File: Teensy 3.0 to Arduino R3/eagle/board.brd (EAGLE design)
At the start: 100 x 55.9 mm, 43 parts, among them IC1 7805TV, IC2 24AA256SN, IC3 24AA256SN, IC4 24AA256SN, IC5 24AA256SN, U1 MICROSD

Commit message: Version 3 final
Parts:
- added C9: (no value), resistor:PANASONIC_D
- added D2: (no value), SparkFun-DiscreteSemi:SMA-DIODE-KIT
- added R10, R11, R12, R13, R14, R15, R16, R17, R18, R19, R20, R21, R22, R23, R24, R5, R6, R7, R8, R9: (no value), resistor:R0805
- added SJ3, SJ4, SJ5, SJ6: (no value), SparkFun-Passives:SJ_2S-NO
- IC1: value 7805TV -> 78XX compatible
- SJ1, SJ2: value SOLDERJUMPERNO -> (none)
- moved SJ2 10.0 mm to (25.4, 39.4)
- moved SJ1 8.47 mm to (20.3, 38.1), turned to 180 degrees
- moved F1 4.62 mm to (17.1, 33.0), turned to 270 degrees
- moved C2 2.62 mm to (27.9, 31.8)
- moved D1 1.27 mm to (21.6, 43.2)
- moved IC1 1.27 mm to (34.3, 38.1)
- moved C1 1.27 mm to (25.4, 43.8)
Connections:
- removed net 3V3: C2.+, C4.1, C5.1, C6.1, C7.1, C8.1, IC1.3, IC2.3, IC2.8, IC3.2, IC3.3, IC3.8, IC4.1, IC4.3, IC4.8, IC5.1, IC5.2, IC5.3, IC5.8, JP12.1, JP13.13, JP14.1, JP6.5, JP6.7, R1.2, R2.2, R3.2, R4.2, SJ2.1, U1.4
- new net N$10: JP2.7, R10.2
- new net N$11: JP2.6, R11.2
- new net N$12: JP2.5, R12.2
- new net N$13: JP1.13, R13.2
- new net N$14: JP1.12, R14.2
- new net N$15: JP1.11, R15.2
- new net N$16: JP1.10, R16.2
- new net N$17: JP1.9, R17.2
- new net N$18: JP1.8, R18.2
- new net N$19: JP1.7, R19.2
- new net N$20: JP1.6, R20.2
- new net N$21: JP2.4, R21.2
- new net N$22: JP2.3, R22.2
- new net N$23: JP2.2, R23.2
- new net N$24: JP2.1, R24.2
- new net N$5: JP1.5, R5.2
- new net N$6: JP1.4, R6.2
- new net N$7: JP1.3, R7.2
- new net N$8: JP1.2, R8.2
- new net N$9: JP1.1, R9.2
- new net NIC: R4.1, SJ3.1, SJ4.1, U1.CD1
- new net QW: SJ5.1, SJ6.1, U1.2
- net 3.3V: now also C2.+, C4.1, C5.1, C6.1, C7.1, C8.1, C9.+, D2.A, IC1.3, IC2.3, IC2.8, IC3.2, IC3.3, IC3.8, IC4.1, IC4.3, IC4.8, IC5.1, IC5.2, IC5.3, IC5.8, JP12.1, JP13.13, JP14.1, JP6.5, JP6.7, R1.2, R2.2, R3.2, R4.2, SJ2.1, U1.4
- net A0: now also R23.1; no longer JP2.2
- net A1: now also R22.1; no longer JP2.3
- net A2: now also R21.1; no longer JP2.4
- net A3: now also R12.1; no longer JP2.5
- net A4: now also R11.1; no longer JP2.6
- net A5: now also R10.1; no longer JP2.7
- net D0: now also R13.1; no longer JP1.13
- net D1: now also R14.1; no longer JP1.12
- net D10: now also R7.1, SJ6.2; no longer JP1.3, U1.2
- net D11: now also R8.1; no longer JP1.2
- net D12: now also R9.1; no longer JP1.1
- net D13: now also R24.1; no longer JP2.1
- net D2: now also R15.1; no longer JP1.11
- net D3: now also R16.1; no longer JP1.10
- net D4: now also R17.1; no longer JP1.9
- net D5: now also R18.1; no longer JP1.8
- net D6: now also R19.1; no longer JP1.7
- net D7: now also R20.1, SJ3.2; no longer JP1.6
- net D8: now also R5.1, SJ4.2; no longer JP1.5, R4.1, U1.CD1
- net D9: now also R6.1, SJ5.2; no longer JP1.4
- net GND: now also C9.-
- net N$3: now also D2.C
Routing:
- net 3.3V: track 0.00 -> 400.0 mm, vias 0 -> 7
- net 3V3: track 390.8 -> 0.00 mm, vias 7 -> 0
- net QW: track 0.00 -> 51.5 mm, vias 0 -> 2
- net NIC: track 0.00 -> 51.1 mm, vias 0 -> 5
- net D8: track 73.9 -> 23.0 mm, vias 5 -> 0
- net D10: track 62.2 -> 23.2 mm, vias 2 -> 0
- net A1: track 29.0 -> 6.03 mm
- net N$22: track 0.00 -> 21.6 mm
- net A3: track 29.0 -> 16.2 mm
- net N$11: track 0.00 -> 12.4 mm
- net A2: track 29.0 -> 16.8 mm
- net N$12: track 0.00 -> 11.1 mm
- net N$21: track 0.00 -> 10.5 mm
- net N$10: track 0.00 -> 9.84 mm
- net D13: track 119.5 -> 113.1 mm
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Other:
- board text added: "-"
- board text added: "D10"
- board text added: "D7"
- board text added: "D8"
- board text added: "D9"
- board text added: "PROGRAM"
- board text added: "SD Card CS"
- board text added: "SD Card dedect"

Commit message: V3-2: fixed several bugs
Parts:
- added C10: (no value), rcl:SANYO-OSCON_SMD_E7
- added JP16: (no value), SparkFun-Connectors:1X02
- C3: device SparkFun-Capacitors:EIA3528-KIT -> rcl:A/3216-18W
- moved C3 17.1 mm to (20.3, 5.08), turned to 90 degrees
- moved R22 16.7 mm to (45.7, 7.62), turned to 90 degrees
- moved F2 7.24 mm to (8.89, 12.1), turned to 180 degrees
- moved JP15 3.42 mm to (3.81, 13.3), turned to 270 degrees
- moved R23 3.18 mm to (39.4, 8.89)
- moved JP6 2.54 mm to (61.0, 3.81)
- moved JP10 1.91 mm to (5.08, 24.8)
- moved X1 1.27 mm to (6.99, 36.8)
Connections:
- new net N$25: C10.+, JP16.2
- net GND: now also C10.-, C3.-; no longer C3.C
- net N$2: now also JP16.1
- net VUSB: now also C3.+; no longer C3.A
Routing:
- net VUSB: track 149.5 -> 128.5 mm, vias 2 -> 0
- net N$22: track 21.6 -> 2.96 mm
- net A1: track 6.03 -> 24.3 mm
- net N$25: track 0.00 -> 8.46 mm
- net GND: track 20.5 -> 14.9 mm, vias 40 -> 42
- net VIN: track 129.7 -> 135.3 mm
- net A0: track 47.8 -> 44.7 mm
- net EXT_RESET: track 51.5 -> 54.1 mm
- net 5V: track 15.0 -> 17.6 mm
- net N$2: track 4.02 -> 6.50 mm
- net N$23: track 2.63 -> 4.91 mm
- net N$1: track 28.4 -> 26.5 mm
- net N$3: track 49.5 -> 47.9 mm
- net PROG: track 104.6 -> 103.2 mm
- net EXT_POWER: track 32.2 -> 33.5 mm
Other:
- board text added: "A4 SDA"
- board text added: "A5 SCL"
- board text added: "MISO 12"
- board text added: "MOSI 11"
- board text added: "PWM 3"
- board text added: "PWM 4"
- board text added: "PWM 5"
- board text added: "PWM 6"
- board text added: "PWM RX2 CS1 9"
- board text added: "PWM TX2 CS0 10"
- board text added: "RX1 0"
- board text added: "RX3 7"
- board text added: "SCK 13"
- board text added: "TX1 1"
- board text added: "TX3 8"
- board text added: "V000003-2 tinytiger.ch"
- board text removed: "0"
- board text removed: "1"
- board text removed: "10"
- board text removed: "11"
- board text removed: "12"
- board text removed: "13"
- board text removed: "3"
- board text removed: "4"
- board text removed: "5"
- board text removed: "6"
- board text removed: "7"
- board text removed: "8"
- board text removed: "9"
- board text removed: "A4"
- board text removed: "A5"
- board text removed: "C3"
- board text removed: "F2"
- board text removed: "V000003 tinytiger.ch"

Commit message: inital commit V4
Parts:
- removed JP14: (no value), SparkFun-Connectors:1X02
- added JP17, JP18: M10", SparkFun-Connectors:1X10
- added R25, R26, R27, R28, R29, R30, R31, R32, R33, R34, R35, R36, R37, R38, R39, R40, R41, R42: (no value), resistor:R0805
- added SJ10, SJ11, SJ12, SJ13, SJ7, SJ8, SJ9: (no value), SparkFun-Passives:SJ_2S-NO
- added U$1: XBEE-1B2, SparkFun-RF:XBEE-SILK
- added U$3, U$4: M24, SparkFun-Connectors:1X24
- C10: device rcl:SANYO-OSCON_SMD_E7 -> rcl:085CS_1AR
- C3: device rcl:A/3216-18W -> rcl:CT3528
- JP12: value (none) -> PINHD-1X10; device adafruit:1X13-BIG -> adafruit:1X10-BIG
- JP13: device adafruit:1X13-BIG -> adafruit:1X08-BIG
- JP16: device SparkFun-Connectors:1X02 -> SparkFun-Connectors:1X05
- JP2: value M14 -> (none); device SparkFun-Connectors:1X14 -> pinhead:2X06
- JP3: value M10" -> M14; device SparkFun-Connectors:1X10 -> SparkFun-Connectors:1X14
- JP4: value M10" -> (none); device SparkFun-Connectors:1X10 -> pinhead:2X06
- moved CN2 106.1 mm to (102.2, 66.0), turned to 90 degrees
- moved S1 96.8 mm to (95.2, 36.8), turned to 270 degrees
- moved JP10 95.5 mm to (86.4, 74.9), turned to 0 degrees
- moved X1 87.7 mm to (92.7, 55.2), turned to 90 degrees
- moved CN1 82.1 mm to (89.5, 55.2), turned to 270 degrees
- moved JP8 80.2 mm to (47.0, 77.5), turned to 0 degrees
- moved F1 79.9 mm to (95.9, 46.4)
- moved JP6 73.8 mm to (64.8, 77.5), turned to 0 degrees
- moved R13 73.3 mm to (5.71, 64.1), turned to 180 degrees
- moved R3 73.0 mm to (90.2, 38.1), flipped to the bottom
- moved D1 69.9 mm to (91.4, 46.4)
- moved R14 69.9 mm to (5.71, 61.6), turned to 180 degrees
- moved SJ1 68.5 mm to (88.3, 47.0), turned to 90 degrees
- moved JP15 66.8 mm to (32.4, 73.7), turned to 90 degrees
- moved R15 66.5 mm to (5.71, 59.1), turned to 180 degrees
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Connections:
- new net N$26: JP17.9, R26.2
- new net N$27: JP17.8, R27.2
- new net N$28: JP17.7, R28.2
- new net N$29: JP17.6, R29.2
- new net N$30: JP17.5, R30.2
- new net N$31: JP17.4, R31.2
- new net N$32: JP17.3, R32.2
- new net N$33: JP17.2, R33.2
- new net N$34: JP17.1, R34.2
- new net N$35: JP3.11, R35.2
- new net N$36: JP3.10, R36.2
- new net N$37: JP3.9, R37.2
- new net N$38: JP3.8, R38.2
- new net N$39: JP18.4, R39.2
- new net N$40: JP18.3, R40.2
- new net N$41: JP18.2, R41.2
- new net N$42: JP18.1, R42.2
- new net N$45: JP13.6, U$1.4
- new net N$46: JP13.5, U$1.5
- new net N$47: JP13.4, U$1.6
- new net N$48: JP13.3, U$1.7
- new net N$49: JP13.2, U$1.8
- new net N$50: JP13.1, U$1.9
- new net N$51: JP12.1, U$1.20
- new net N$52: JP4.10, JP4.9, SJ10.1, SJ11.1, SJ12.1, SJ9.1
- new net N$53: JP4.11, JP4.12
- new net N$54: JP12.2, U$1.19
- new net N$55: JP12.3, U$1.18
- new net N$56: JP12.4, U$1.17
- new net N$57: JP2.7, JP2.8
- new net N$58: JP2.10, JP2.9
- new net N$59: JP12.5, U$1.16
- new net N$60: JP12.6, U$1.15
- new net N$61: JP12.7, U$1.14
- new net N$62: JP12.8, U$1.13
- new net N$63: JP12.9, U$1.12
- new net N$64: JP12.10, U$1.11
- net 3.3V: now also JP16.4, JP2.3, JP2.4, JP2.5, JP2.6, JP3.12, SJ13.1, U$1.1, U$4.23; no longer JP12.1, JP13.13, JP14.1, JP2.12
- net 5V: now also SJ13.2; no longer JP14.2
- net A0: now also U$4.13
- net A1: now also U$4.14
- net A10: now also R42.1, U$4.2; no longer JP13.6, JP4.1
- net A11: now also R41.1, U$4.3; no longer JP13.7, JP4.2
- net A12: now also R40.1, U$4.4; no longer JP13.8, JP4.3
- net A13: now also R39.1, U$4.5; no longer JP13.9, JP4.4
- net A2: now also U$4.15
- net A3: now also U$4.16
- net A4: now also U$4.17
- net A5: now also U$4.18
- net A6: now also R38.1, U$4.19; no longer JP13.2, JP2.8
- net A7: now also R37.1, U$4.20; no longer JP13.3, JP2.9
- net A8: now also R36.1, U$4.21; no longer JP13.4, JP2.10
- net A9: now also R35.1, U$4.22; no longer JP13.5, JP2.11
- net AGND: now also JP3.13, U$4.24; no longer JP12.12, JP2.13
- net AREF: now also JP18.6, U$4.7; no longer JP4.6
- net D0: now also JP13.8, U$1.2, U$3.24
- net D1: now also JP13.7, U$1.3, U$3.23
- net D10: now also SJ10.2, U$3.14
- net D11: now also JP2.11, JP2.12, JP4.5, JP4.6, U$3.13
- net D12: now also U$3.12
- net D13: now also JP4.7, JP4.8, U$4.12
- net D2: now also SJ11.2, SJ7.2, U$3.22
- net D24: now also R25.1, U$3.11; no longer JP12.2, JP3.10
- net D25: now also R26.1, U$3.10; no longer JP12.3, JP3.9
- net D26: now also R27.1, U$3.9; no longer JP12.4, JP3.8
- net D27: now also R28.1, U$3.8; no longer JP12.5, JP3.7
- net D28: now also R29.1, U$3.7; no longer JP12.6, JP3.6
- net D29: now also R30.1, U$3.6; no longer JP12.7, JP3.5
- net D3: now also SJ12.2, SJ8.2, U$3.21
- net D30: now also R31.1, U$3.5; no longer JP12.8, JP3.4
- net D31: now also R32.1, U$3.4; no longer JP12.9, JP3.3
- net D32: now also R33.1, U$3.3; no longer JP12.10, JP3.2
- net D33: now also R34.1, U$3.2; no longer JP12.11, JP3.1
- net D4: now also U$3.20
- net D5: now also U$3.19
- net D6: now also U$3.18
- net D7: now also U$3.17
- net D8: now also U$3.16
- net D9: now also SJ9.2, U$3.15
- net GND: now also JP16.3, JP18.9, JP2.1, JP2.2, JP4.1, JP4.2, JP4.3, JP4.4, U$1.10, U$3.25, U$4.10; no longer JP12.13, JP13.1, JP4.9
- net N$10: now also JP3.7; no longer JP2.7
- net N$11: now also JP3.6; no longer JP2.6
- net N$12: now also JP3.5; no longer JP2.5
- net N$2: now also C10.+; no longer JP16.1
- net N$21: now also JP3.4; no longer JP2.4
- net N$22: now also JP3.3; no longer JP2.3
- net N$23: now also JP3.2; no longer JP2.2
- net N$24: now also JP3.1; no longer JP2.1
- net N$25: now also JP17.10, R25.2; no longer C10.+, JP16.2
- net PROG: now also JP16.2, JP18.5, U$4.6; no longer JP13.10, JP4.5
- net QW: now also SJ7.1, SJ8.1
- net RESET: now also JP16.1, JP18.7, U$4.8; no longer JP4.7
- net VBAT: now also JP16.5, JP18.10, U$4.11; no longer JP13.12, JP4.10
- net VIN: now also JP3.14, U$4.25; no longer JP2.14
- net VUSB: now also JP18.8, U$4.9; no longer JP13.11, JP4.8
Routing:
- net D0: track 23.3 -> 196.9 mm, vias 0 -> 5
- net D3: track 23.3 -> 167.9 mm, vias 0 -> 7
- net D9: track 22.6 -> 146.2 mm, vias 0 -> 5
- net D8: track 23.0 -> 133.6 mm, vias 0 -> 4
- net D1: track 23.3 -> 133.6 mm, vias 0 -> 5
- net N$45: track 0.00 -> 109.8 mm, vias 0 -> 4
- net D11: track 101.1 -> 202.4 mm
- net D33: track 90.3 -> 2.96 mm
- net D10: track 23.2 -> 109.7 mm, vias 0 -> 7
- net D32: track 85.9 -> 2.96 mm
- net A13: track 85.2 -> 2.96 mm, vias 2 -> 0
- net A11: track 84.4 -> 2.96 mm, vias 2 -> 0
- net A10: track 84.4 -> 2.96 mm, vias 1 -> 0
- net A12: track 83.7 -> 2.96 mm, vias 2 -> 0
- net D4: track 23.3 -> 102.2 mm, vias 0 -> 3
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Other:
- board size 100 x 55.9 mm -> 100 x 80 mm
- board text added: "GND 0 1 2 3 4 5 6 7 8 9 10 11 12 24 25 26 27 28 29 30 31 32 33"
- board text added: "REV. V000004"
- board text added: "Teensy 3.0"
- board text added: "VIN AGND 3V3 A9 A8 A7 A6 A5 A4 A3 A2 A1 A0 13 VBAT GND VUSB RST AREF PRG A13 A12 A11 A10"
- board text added: "WIZ820io"
- board text added: "XBee"
- board text added: "github.com/thewknd/Teensy3.0ToArduinoR3"
- board text added: "tinytiger.ch"
- board text removed: "24"
- board text removed: "25"
- board text removed: "26"
- board text removed: "27"
- board text removed: "28"
- board text removed: "29"
- board text removed: "30"
- board text removed: "31"
- board text removed: "32"
- board text removed: "33"
- board text removed: "A10"
- board text removed: "A11"
- board text removed: "A12"
- board text removed: "A13"
- board text removed: "A6"
- board text removed: "A7"
- board text removed: "A8"
- board text removed: "A9"
- board text removed: "AGND"
- board text removed: "C1"
- board text removed: "D1"
- board text removed: "D10"
- board text removed: "D7"
- board text removed: "D8"
- board text removed: "D9"
- board text removed: "I2C Pullup"
- board text removed: "PROG"
- board text removed: "PROGRAM"
- board text removed: "REG."
- board text removed: "RESET"
- board text removed: "SD Card CS"
- board text removed: "SD Card dedect"
- board text removed: "SJ1"
- board text removed: "SJ2"
- board text removed: "V000003-2 tinytiger.ch"
- board text removed: "VBAT"
- board text removed: "VUSB"

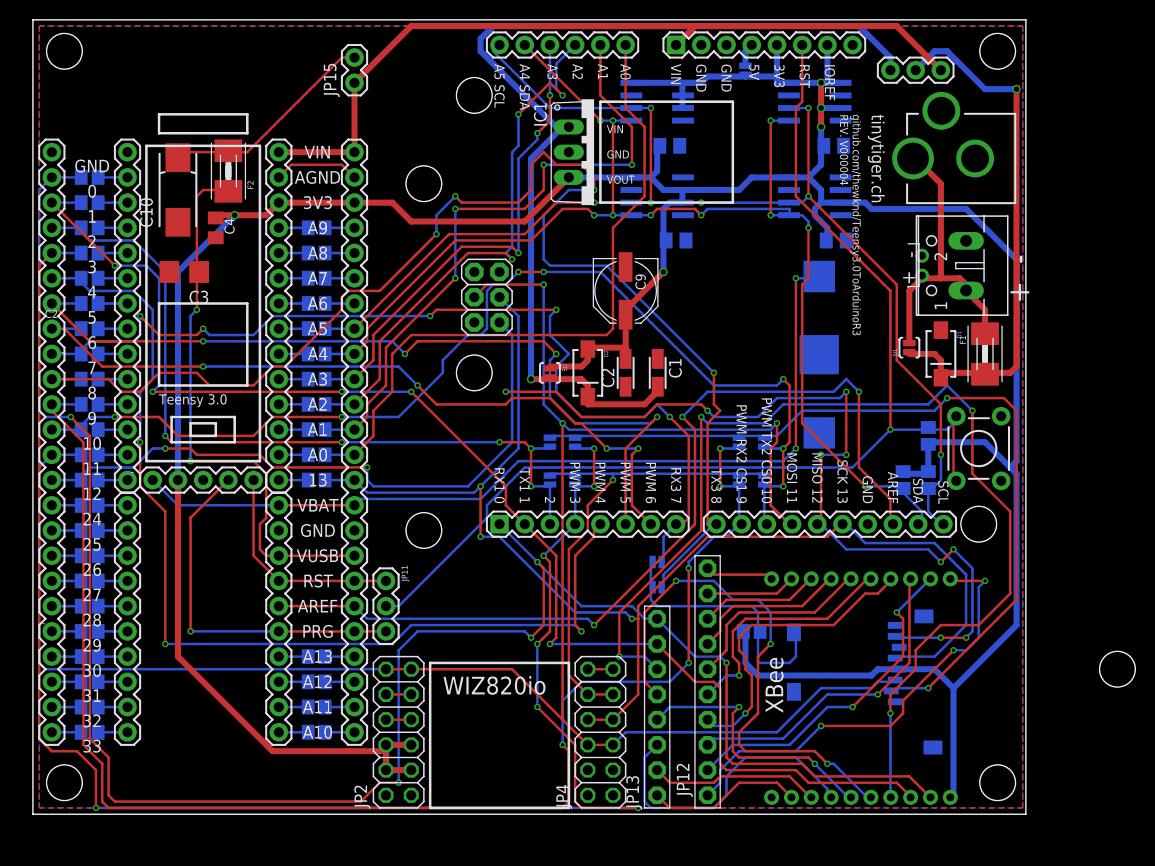
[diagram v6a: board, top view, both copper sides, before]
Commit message: -added RS485 transceiver
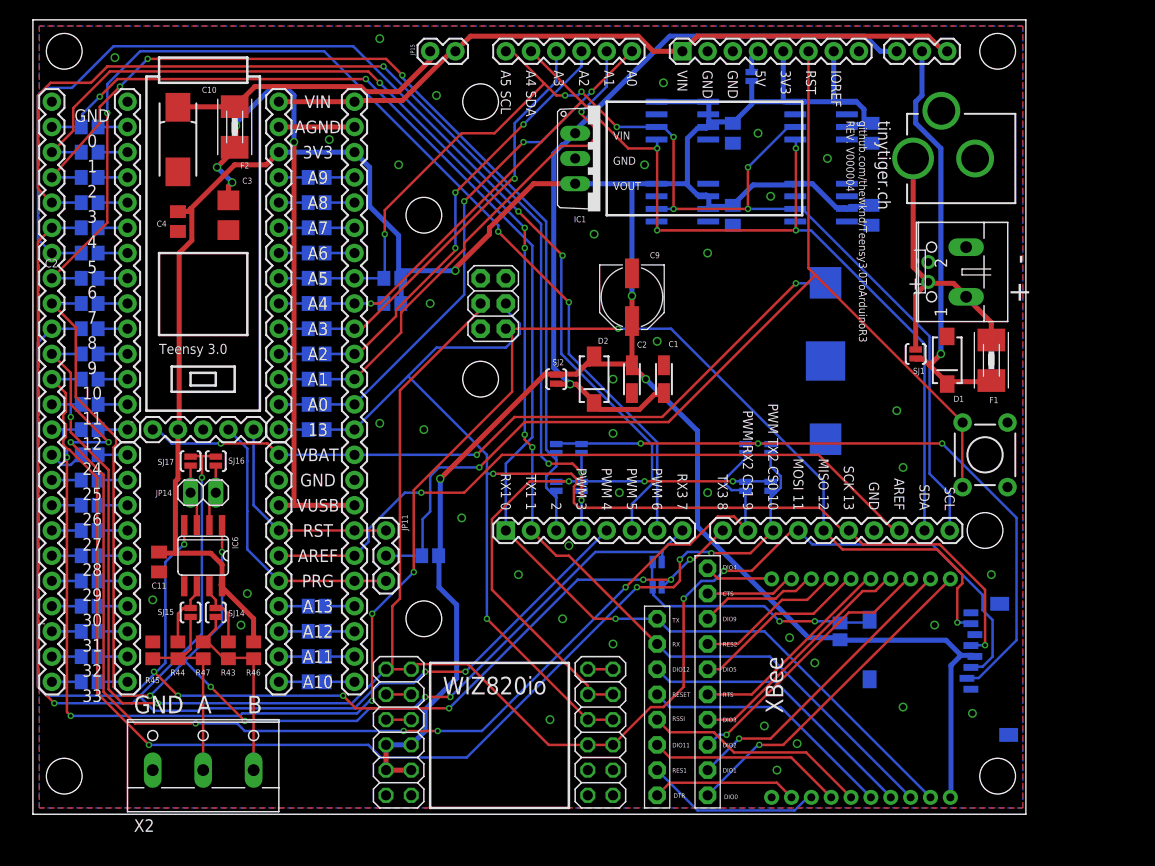
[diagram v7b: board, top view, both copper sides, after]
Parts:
- added C11: (no value), rcl:C0805K
- added IC6: LTC2862, maxim:SO08
- added JP14: (no value), pinhead:1X02
- added R43, R44, R45, R46, R47: (no value), resistor:R0805
- added SJ14, SJ15, SJ16, SJ17: (no value), SparkFun-Passives:SJ_2S-NO
- added X2: (no value), con-wago-508:W237-133
- moved R2 57.7 mm to (36.2, 54.0), turned to 180 degrees
- moved R1 54.4 mm to (36.2, 51.4), turned to 180 degrees
- moved R3 51.6 mm to (40.0, 26.0), turned to 180 degrees
- moved JP15 10.6 mm to (42.5, 76.8), turned to 180 degrees
- moved R4 8.89 mm to (81.3, 18.4), turned to 270 degrees
- moved U1 7.73 mm to (83.8, 21.6)
- moved C3 7.24 mm to (19.7, 60.3), turned to 270 degrees
- moved C8 6.48 mm to (70.5, 68.6), turned to 270 degrees
- moved C6 6.25 mm to (70.5, 60.3), turned to 270 degrees
- moved R11 5.08 mm to (28.6, 51.4)
- moved R12 5.08 mm to (28.6, 48.9)
- moved R15 5.08 mm to (5.71, 64.1)
- moved R20 5.08 mm to (5.71, 51.4)
- moved R35 5.08 mm to (28.6, 64.1)
- moved R5 5.08 mm to (5.71, 48.9)
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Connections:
- new net N$43: IC6.2, JP14.2, SJ16.2
- new net N$44: IC6.3, JP14.1, SJ17.2
- new net N$65: IC6.7, R43.1, SJ14.1
- new net N$66: IC6.6, R44.1, SJ15.1
- new net RS485A: R44.2, R45.2, R47.1, SJ15.2, X2.2
- new net RS485B: R43.2, R46.1, R47.2, SJ14.2, X2.3
- net 3.3V: now also C11.1, IC6.8, R46.2
- net D4: now also SJ16.1, SJ17.1
- net D7: now also IC6.1
- net D8: now also IC6.4
- net GND: now also C11.2, IC6.5, R45.1, X2.1
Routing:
- net N$45: track 109.8 -> 28.8 mm, vias 4 -> 0
- net D3: track 167.9 -> 109.7 mm, vias 7 -> 4
- net D0: track 196.9 -> 141.8 mm, vias 5 -> 3
- net D4: track 102.2 -> 145.6 mm, vias 3 -> 4
- net D6: track 76.2 -> 110.2 mm, vias 4 -> 3
- net D7: track 96.6 -> 130.3 mm, vias 5 -> 6
- net D5: track 85.8 -> 115.4 mm, vias 4 -> 2
- net N$46: track 54.2 -> 25.8 mm, vias 3 -> 0
- net N$3: track 100.5 -> 77.0 mm
- net AREF: track 93.0 -> 70.6 mm, vias 3 -> 1
- net RS485A: track 0.00 -> 21.4 mm
- net RS485B: track 0.00 -> 20.3 mm
- net D2: track 79.3 -> 99.6 mm, vias 5 -> 3
- net D12: track 152.1 -> 172.0 mm, vias 11 -> 7
- net D10: track 109.7 -> 128.0 mm, vias 7 -> 4
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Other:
- board text added: "A"
- board text added: "B"
- board text added: "CTS"
- board text added: "D10"
- board text added: "D2"
- board text added: "D3"
- board text added: "D9"
- board text added: "DIO0"
- board text added: "DIO1"
- board text added: "DIO11"
- board text added: "DIO12"
- board text added: "DIO2"
- board text added: "DIO3"
- board text added: "DIO4"
- board text added: "DIO5"
- board text added: "DIO9"
- board text added: "DTR"
- board text added: "RES1"
- board text added: "RES2"
- board text added: "RESET"
- board text added: "RSSI"
- board text added: "RTS"
- board text added: "RX"
- board text added: "SD slave select"
- board text added: "TX"
- board text added: "XBee slave select"
